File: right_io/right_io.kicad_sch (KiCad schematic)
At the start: 0 parts

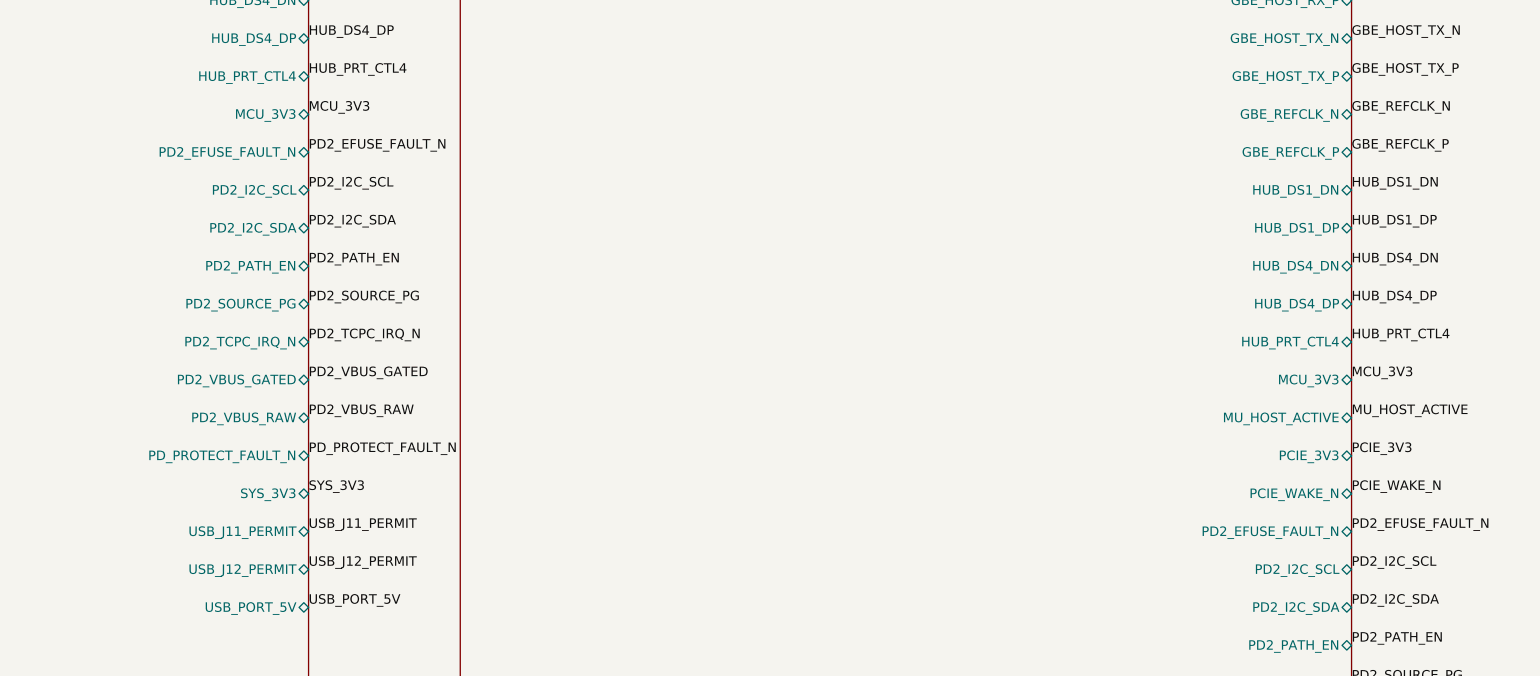
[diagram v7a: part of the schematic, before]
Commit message: rework the board placement and fix more power stuff
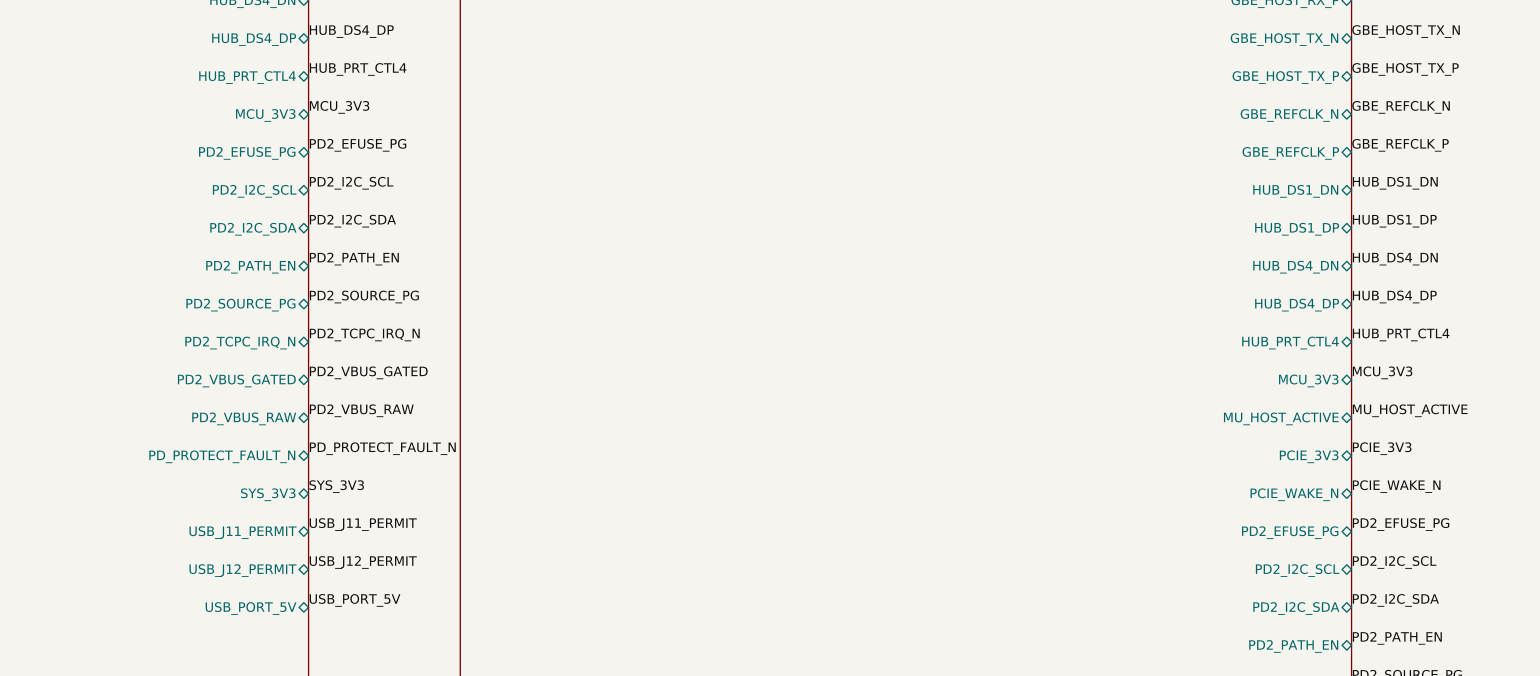
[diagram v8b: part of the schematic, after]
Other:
- sheet FPC-2 (to Center) ports: added PD2_EFUSE_PG; removed PD2_EFUSE_FAULT_N
- sheet PD2 Dual-Role ports: added PD2_EFUSE_PG; removed PD2_EFUSE_FAULT_N
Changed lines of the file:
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@@
 (sheet
   (at 30.48 39.37)
-  (size 119.38 149.86)
+  (size 119.38 149.8600)
   (stroke (width 0.1524) (type solid))
   (fill (color 0 0 0 0.0))
@@
     (effects (font (size 1.27 1.27)) (justify left))
   )
-  (pin "PD2_EFUSE_FAULT_N" bidirectional
+  (pin "PD2_EFUSE_PG" bidirectional
     (at 149.86 74.93 0)
     (effects (font (size 1.27 1.27)) (justify left))
@@
 (sheet
   (at 30.48 219.71)
-  (size 119.38 149.86)
+  (size 119.38 149.8600)
   (stroke (width 0.1524) (type solid))
   (fill (color 0 0 0 0.0))
@@
 (sheet
   (at 30.48 400.05)
-  (size 119.38 149.86)
+  (size 119.38 149.8600)
   (stroke (width 0.1524) (type solid))
   (fill (color 0 0 0 0.0))
@@
 (sheet
   (at 170.18 39.37)
-  (size 119.38 223.52)
+  (size 119.38 223.5200)
   (stroke (width 0.1524) (type solid))
   (fill (color 0 0 0 0.0))
@@
     (effects (font (size 1.27 1.27)) (justify left))
   )
-  (pin "PD2_EFUSE_FAULT_N" bidirectional
+  (pin "PD2_EFUSE_PG" bidirectional
     (at 289.56 125.73 0)
     (effects (font (size 1.27 1.27)) (justify left))
@@
   (effects (font (size 1.27 1.27)) (justify left bottom))
 )
-(label "PD2_EFUSE_FAULT_N"
+(label "PD2_EFUSE_PG"
   (at 149.86 74.93 0)
   (effects (font (size 1.27 1.27)) (justify left bottom))
@@
   (effects (font (size 1.27 1.27)) (justify left bottom))
 )
-(label "PD2_EFUSE_FAULT_N"
+(label "PD2_EFUSE_PG"
   (at 289.56 125.73 0)
   (effects (font (size 1.27 1.27)) (justify left bottom))
